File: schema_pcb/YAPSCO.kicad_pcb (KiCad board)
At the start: 2 copper layers, 82.8 x 73.2 mm, 80 parts, among them J1 DB15_Female, J2 DB9_Female_MountingHoles, K1 Supply, K3 FautlPol, P1 STEP, P2 DIR, P3 CONN, P4 ENABLE, P5 +-10V, P6 InOut, P7 Jumper, P8 Jumper, P9 Jumper, Q1 NPN, U1 7805, U10 MC33063AD, U2 dsPIC30F4012, U3 6N137, U4 6N137, U5 6N137, U6 LM358, U7 74HC14, U8 LM339D, U9 L7812

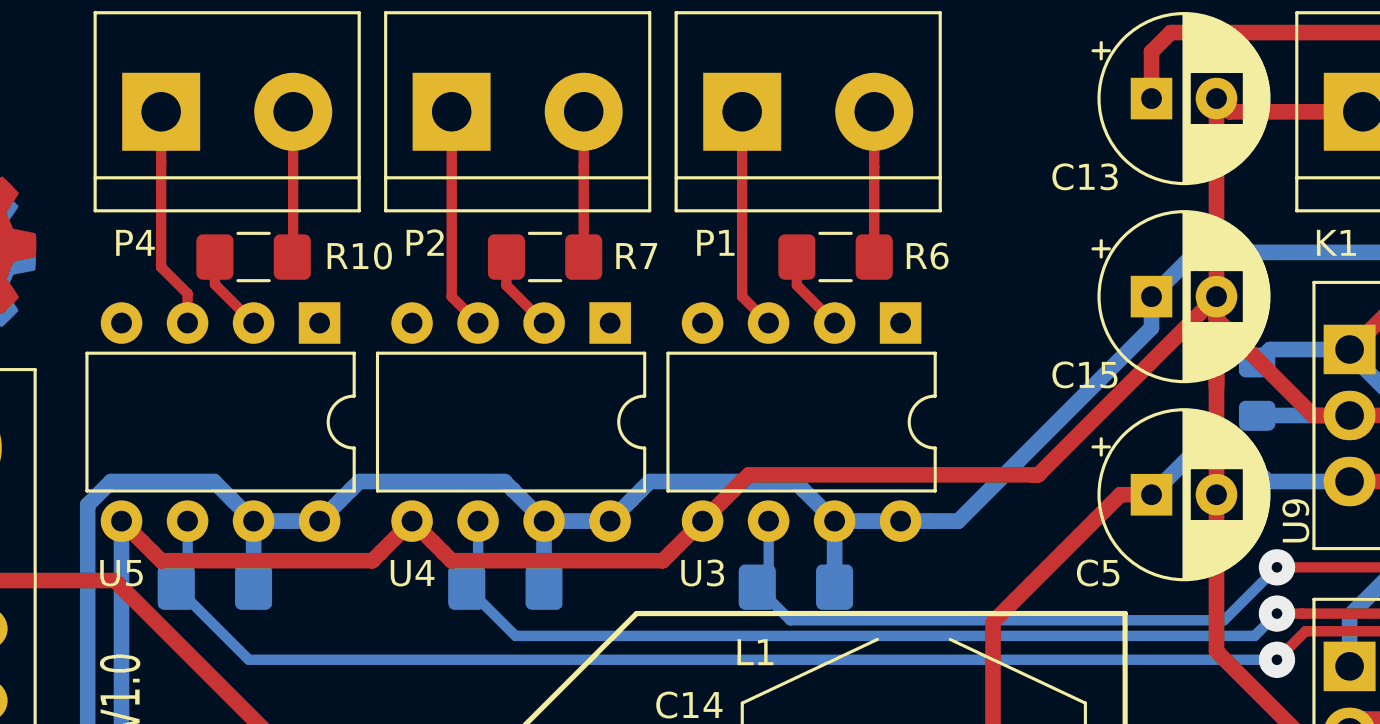
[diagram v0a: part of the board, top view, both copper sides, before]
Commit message: Added keep-out area around opto-isolators
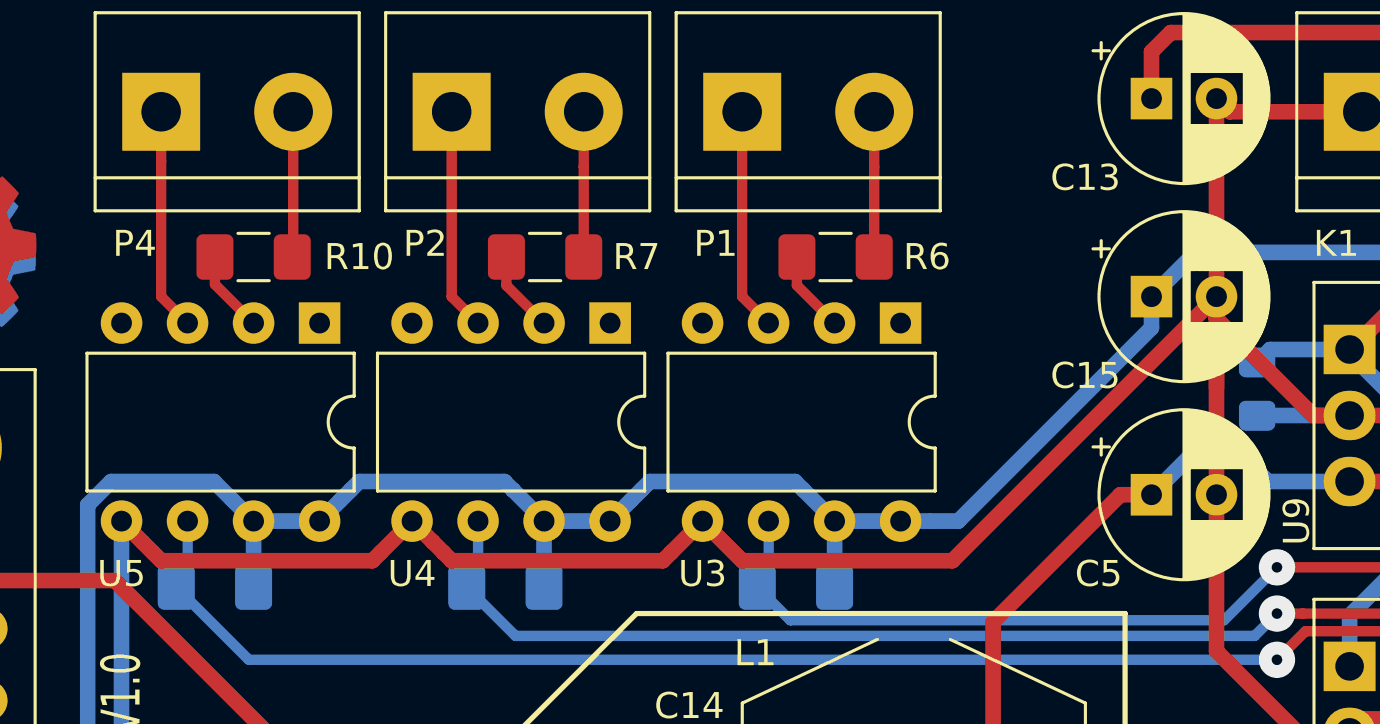
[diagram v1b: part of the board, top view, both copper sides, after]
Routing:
- net GND: track 457.9 -> 459.2 mm
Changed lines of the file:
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@@
     (thickness 1.6)
     (drawings 60)
-    (tracks 1035)
+    (tracks 1032)
     (zones 0)
     (modules 80)
@@
   (segment (start 124.647201 92.135201) (end 124.243999 91.731999) (width 0.6) (layer F.Cu) (net 1))
   (segment (start 134.62 90.932) (end 133.416799 92.135201) (width 0.6) (layer F.Cu) (net 1))
-  (segment (start 145.796 90.932) (end 146.999201 89.728799) (width 0.6) (layer F.Cu) (net 1))
   (segment (start 168.688 99.06) (end 170.688 99.06) (width 0.6) (layer B.Cu) (net 1))
   (segment (start 145.055262 99.06) (end 168.688 99.06) (width 0.6) (layer B.Cu) (net 1))
@@
   (segment (start 182.119 117.348) (end 181.992 117.475) (width 0.6) (layer F.Cu) (net 1))
   (segment (start 184.404 117.348) (end 182.119 117.348) (width 0.6) (layer F.Cu) (net 1))
-  (segment (start 158.71 89.154) (end 165.568 82.296) (width 0.6) (layer F.Cu) (net 1))
-  (segment (start 158.496 89.154) (end 158.71 89.154) (width 0.6) (layer F.Cu) (net 1))
-  (segment (start 147.574 89.154) (end 158.496 89.154) (width 0.6) (layer F.Cu) (net 1))
-  (segment (start 146.999201 89.728799) (end 147.574 89.154) (width 0.6) (layer F.Cu) (net 1))
   (segment (start 136.144 92.456) (end 135.823201 92.135201) (width 0.6) (layer F.Cu) (net 1))
   (segment (start 144.592799 92.135201) (end 144.272 92.456) (width 0.6) (layer F.Cu) (net 1))
@@
   (segment (start 187.207 90.932) (end 191.046011 87.092989) (width 0.6) (layer F.Cu) (net 1))
   (segment (start 191.046011 87.092989) (end 191.046011 81.706101) (width 0.6) (layer F.Cu) (net 1))
+  (segment (start 155.408 92.456) (end 165.568 82.296) (width 0.6) (layer F.Cu) (net 1))
+  (segment (start 145.796 90.932) (end 147.32 92.456) (width 0.6) (layer F.Cu) (net 1))
+  (segment (start 147.32 92.456) (end 155.408 92.456) (width 0.6) (layer F.Cu) (net 1))
   (segment (start 170.688 89.408) (end 170.7355 89.408) (width 0.6) (layer B.Cu) (net 2))
   (segment (start 156.9355 110.2725) (end 156.972 110.236) (width 0.6) (layer F.Cu) (net 2))
@@
   (segment (start 130.048 75.184) (end 130.048 80.7355) (width 0.4) (layer F.Cu) (net 37))
   (segment (start 124.968 77.084) (end 124.968 75.184) (width 0.4) (layer F.Cu) (net 38))
-  (segment (start 124.968 81.16463) (end 124.968 77.084) (width 0.4) (layer F.Cu) (net 38))
-  (segment (start 125.984 82.18063) (end 124.968 81.16463) (width 0.4) (layer F.Cu) (net 38))
-  (segment (start 125.984 83.312) (end 125.984 82.18063) (width 0.4) (layer F.Cu) (net 38))
+  (segment (start 125.984 83.312) (end 124.968 82.296) (width 0.4) (layer F.Cu) (net 38))
+  (segment (start 124.968 82.296) (end 124.968 77.084) (width 0.4) (layer F.Cu) (net 38))
   (segment (start 135.128 104.648) (end 135.128 107.188) (width 0.4) (layer B.Cu) (net 39))
   (segment (start 134.328001 103.848001) (end 135.128 104.648) (width 0.4) (layer B.Cu) (net 39))
@@
       )
     )
+  )
+  (zone (net 0) (net_name "") (layers F&B.Cu) (hatch edge 0.508)
+    (connect_pads (clearance 0.2))
+    (min_thickness 0.254)
+    (keepout (tracks allowed) (vias allowed) (copperpour not_allowed))
+    (fill (arc_segments 32) (thermal_gap 0.508) (thermal_bridge_width 0.508))
+    (polygon
+      (pts
+        (xy 121.412 88.138) (xy 122.428 89.154) (xy 155.194 89.154) (xy 156.21 88.138) (xy 156.21 68.326)
+        (xy 121.412 68.326)
+      )
+    )
